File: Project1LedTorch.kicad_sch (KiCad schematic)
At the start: 5 parts, among them SW1 SW_DPDT_x2, U1 NA555_NL

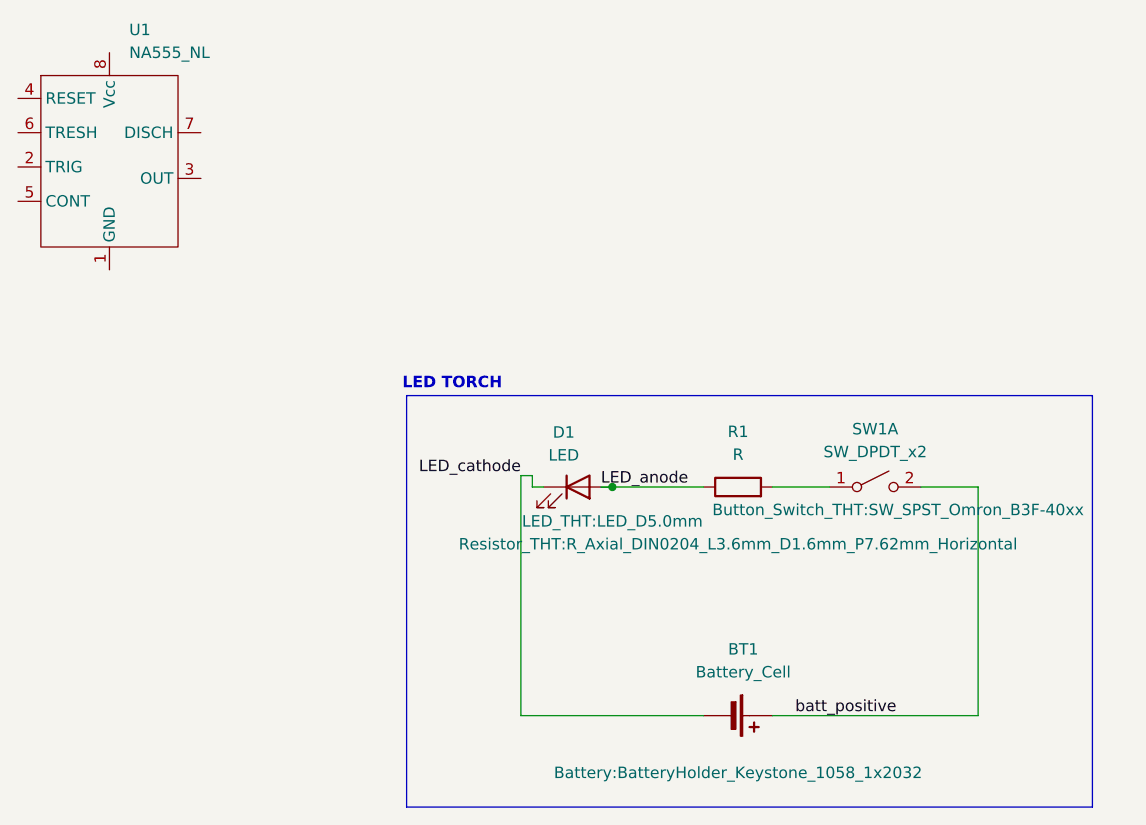
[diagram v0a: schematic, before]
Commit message: Change R to R_US
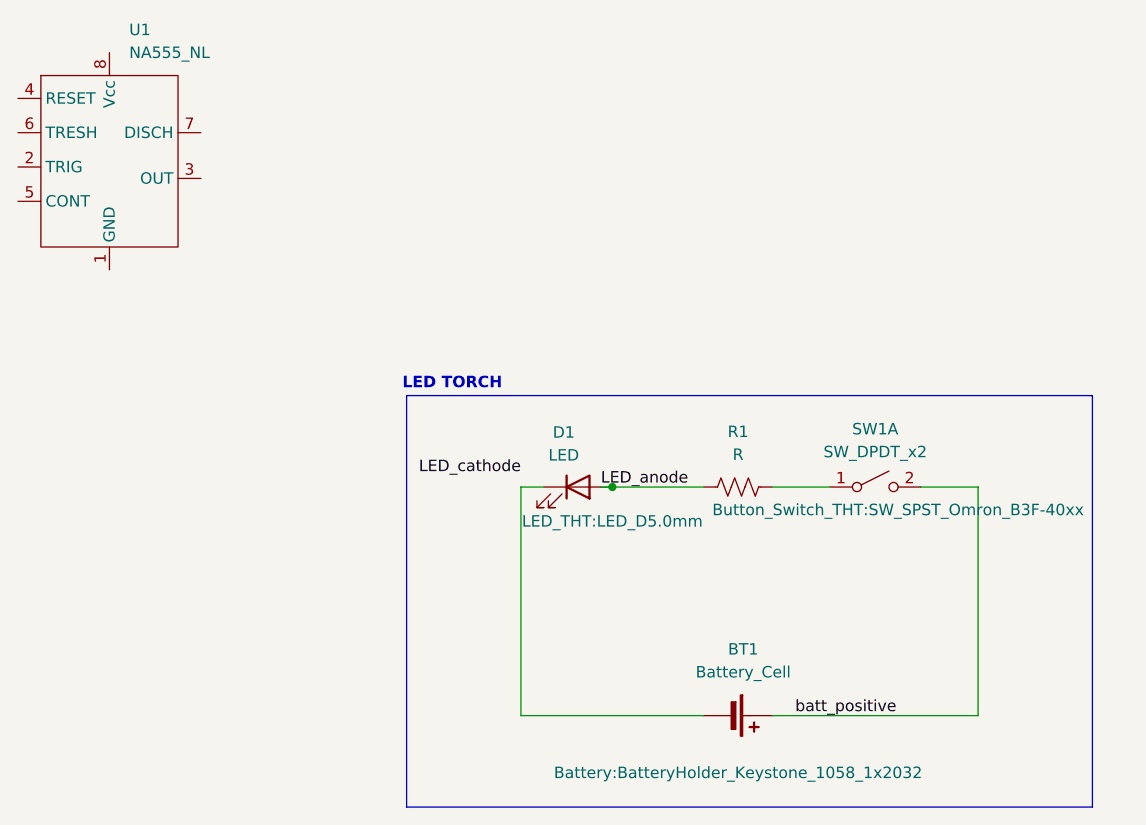
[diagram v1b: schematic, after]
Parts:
- R1: footprint Resistor_THT:R_Axial_DIN0204_L3.6mm_D1.6mm_P7.62mm_Horizontal -> Resistor_SMD:R_0815_2038Metric; symbol Device:R -> Device:R_US
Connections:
- net LED_cathode: no longer BT1.2 (-), D1.1 (K)
- new net: BT1.2 (-), D1.1 (K)
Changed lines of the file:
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@@
 	(wire
 		(pts
-			(xy 128.27 87.63) (xy 128.27 88.9)
+			(xy 127 88.9) (xy 127 114.3)
 		)
 		(stroke
@@
 	(wire
 		(pts
-			(xy 127 87.63) (xy 127 114.3)
-		)
-		(stroke
-			(width 0)
-			(type default)
-		)
-	)
-	(wire
-		(pts
-			(xy 128.27 87.63) (xy 127 87.63)
+			(xy 127 88.9) (xy 129.54 88.9)
 		)
 		(stroke
@@
 		(pts
 			(xy 135.89 88.9) (xy 137.16 88.9)
-		)
-		(stroke
-			(width 0)
-			(type default)
-		)
-	)
-	(wire
-		(pts
-			(xy 128.27 88.9) (xy 129.54 88.9)
 		)
 		(stroke
@@
 	)
 	(symbol
-		(lib_id "Device:R")
+		(lib_id "Device:R_US")
 		(at 151.13 88.9 90)
 		(unit 1)
@@
 			)
 		)
-		(property "Footprint" "Resistor_THT:R_Axial_DIN0204_L3.6mm_D1.6mm_P7.62mm_Horizontal"
-			(at 151.13 95.25 90)
-			(effects
-				(font
-					(size 1.27 1.27)
-				)
+		(property "Footprint" "Resistor_SMD:R_0815_2038Metric"
+			(at 151.384 87.884 90)
+			(effects
+				(font
+					(size 1.27 1.27)
+				)
+				(hide yes)
 			)
 		)
@@
 			)
 		)
-		(property "Description" "Resistor"
+		(property "Description" "Resistor, US symbol"
 			(at 151.13 88.9 0)
 			(effects
@@
 			)
 		)
+		(property "Purpose" ""
+			(at 151.13 88.9 0)
+			(effects
+				(font
+					(size 1.27 1.27)
+				)
+			)
+		)

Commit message: Added R8.
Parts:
- removed U1: NA555_NL, Package_DIP:DIP-8_W7.62mm, symbol NA555_CU:NA555_NL
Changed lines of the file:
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@@
 	(wire
 		(pts
-			(xy 127 114.3) (xy 147.32 114.3)
-		)
-		(stroke
-			(width 0)
-			(type default)
-		)
-	)
-	(wire
-		(pts
-			(xy 171.45 88.9) (xy 177.8 88.9)
-		)
-		(stroke
-			(width 0)
-			(type default)
-		)
-	)
-	(wire
-		(pts
-			(xy 154.94 114.3) (xy 177.8 114.3)
+			(xy 124.46 114.3) (xy 147.32 114.3)
+		)
+		(stroke
+			(width 0)
+			(type default)
+		)
+	)
+	(wire
+		(pts
+			(xy 171.45 88.9) (xy 181.61 88.9)
+		)
+		(stroke
+			(width 0)
+			(type default)
+		)
+	)
+	(wire
+		(pts
+			(xy 154.94 114.3) (xy 181.61 114.3)
 		)
 		(stroke
@@
 	(wire
 		(pts
-			(xy 127 88.9) (xy 127 114.3)
-		)
-		(stroke
-			(width 0)
-			(type default)
-		)
-	)
-	(wire
-		(pts
-			(xy 127 88.9) (xy 129.54 88.9)
-		)
-		(stroke
-			(width 0)
-			(type default)
-		)
-	)
-	(wire
-		(pts
-			(xy 177.8 114.3) (xy 177.8 88.9)
+			(xy 124.46 88.9) (xy 124.46 114.3)
+		)
+		(stroke
+			(width 0)
+			(type default)
+		)
+	)
+	(wire
+		(pts
+			(xy 124.46 88.9) (xy 129.54 88.9)
+		)
+		(stroke
+			(width 0)
+			(type default)
+		)
+	)
+	(wire
+		(pts
+			(xy 181.61 114.3) (xy 181.61 88.9)
 		)
 		(stroke
@@
 					(unit 1)
 				)
-			)
-		)
-	)
-	(symbol
-		(lib_id "NA555_CU:NA555_NL")
-		(at 81.28 49.53 0)
-		(unit 1)
-		(exclude_from_sim no)
-		(in_bom yes)
-		(on_board yes)
-		(dnp no)
-		(fields_autoplaced yes)
-		(property "Reference" "U1"
-			(at 83.4741 38.1 0)
-			(effects
-				(font
-					(size 1.27 1.27)
-				)
-				(justify left)
-			)
-		)
-		(property "Value" "NA555_NL"
-			(at 83.4741 40.64 0)
-			(effects
-				(font
-					(size 1.27 1.27)
-				)
-				(justify left)
-			)
-		)
-		(property "Footprint" "Package_DIP:DIP-8_W7.62mm"
-			(at 104.902 40.894 0)
-			(effects
-				(font
-					(size 1.27 1.27)
-				)
-				(hide yes)
-			)
-		)
-		(property "Datasheet" "https://www.ti.com/lit/ds/symlink/ne555.pdf"
-			(at 105.664 64.516 0)
-			(effects
-				(font
-					(size 1.27 1.27)
-				)
-				(hide yes)
-			)
-		)
-		(property "Description" "New Library created symbol"
-			(at 65.278 65.786 0)
-			(effects
-				(font
-					(size 1.27 1.27)
-				)
-				(hide yes)
-			)
-		)
-		(pin "3"
-		)
-		(pin "7"
-		)
-		(pin "2"
-		)
-		(pin "8"
-		)
-		(pin "1"
-		)
-		(pin "4"
-		)
-		(pin "5"
-		)
-		(pin "6"
-		)
-		(instances
-			(project ""
-				(path "/f64fce91-1a45-4290-821e-720d0742f49b"
-					(reference "U1")
-					(unit 1)
-				)
